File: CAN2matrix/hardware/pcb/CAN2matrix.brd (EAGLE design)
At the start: 41 parts, among them IC1 MEGA8-P, IC2 MCP2515-E/P, IC3 MCP2515-E/P, U1 MCP2551P, U2 MCP2551P, X1 CAN1, X2 CAN2

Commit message: remove erroneous connection between GND and power supply wire at C10
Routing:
- net N$33: track 27.7 -> 28.5 mm
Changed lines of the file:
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@@
 <grid distance="0.05" unitdist="inch" unit="inch" style="lines" multiple="1" display="no" altdistance="0.025" altunitdist="inch" altunit="inch"/>
 <layers>
-<layer number="1" name="Top" color="4" fill="1" visible="yes" active="yes"/>
+<layer number="1" name="Top" color="4" fill="1" visible="no" active="yes"/>
 <layer number="16" name="Bottom" color="1" fill="1" visible="yes" active="yes"/>
 <layer number="17" name="Pads" color="2" fill="1" visible="yes" active="yes"/>
@@
 <wire x1="13.97" y1="72.39" x2="19.05" y2="72.39" width="1.778" layer="16"/>
 <wire x1="19.05" y1="72.39" x2="25.4" y2="72.39" width="1.778" layer="16"/>
-<wire x1="25.4" y1="72.39" x2="26.67" y2="71.12" width="1.778" layer="16"/>
+<wire x1="25.4" y1="72.39" x2="29.21" y2="72.39" width="1.778" layer="16"/>
 <contactref element="SV3" pad="3"/>
-<wire x1="26.67" y1="71.12" x2="26.67" y2="64.77" width="1.778" layer="16"/>
-<wire x1="26.67" y1="64.77" x2="27.94" y2="63.5" width="1.778" layer="16"/>
-<wire x1="27.94" y1="63.5" x2="30.48" y2="63.5" width="1.778" layer="16"/>
+<wire x1="29.21" y1="72.39" x2="29.21" y2="64.77" width="1.778" layer="16"/>
+<wire x1="29.21" y1="64.77" x2="30.48" y2="63.5" width="1.778" layer="16"/>
 </signal>
 </signals>

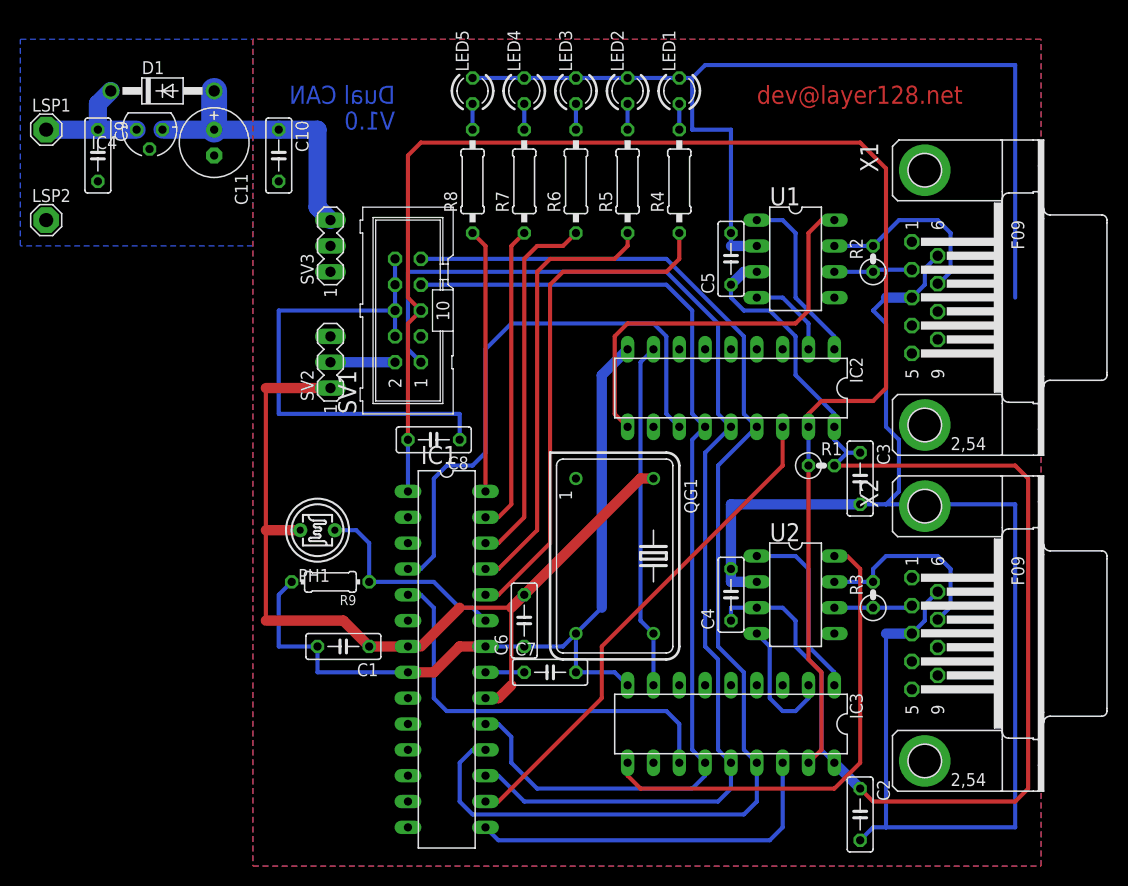
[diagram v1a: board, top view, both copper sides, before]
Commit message: rework top layer to avoid shortcuts with Sub-D connector; solve overlapping error with connector pad
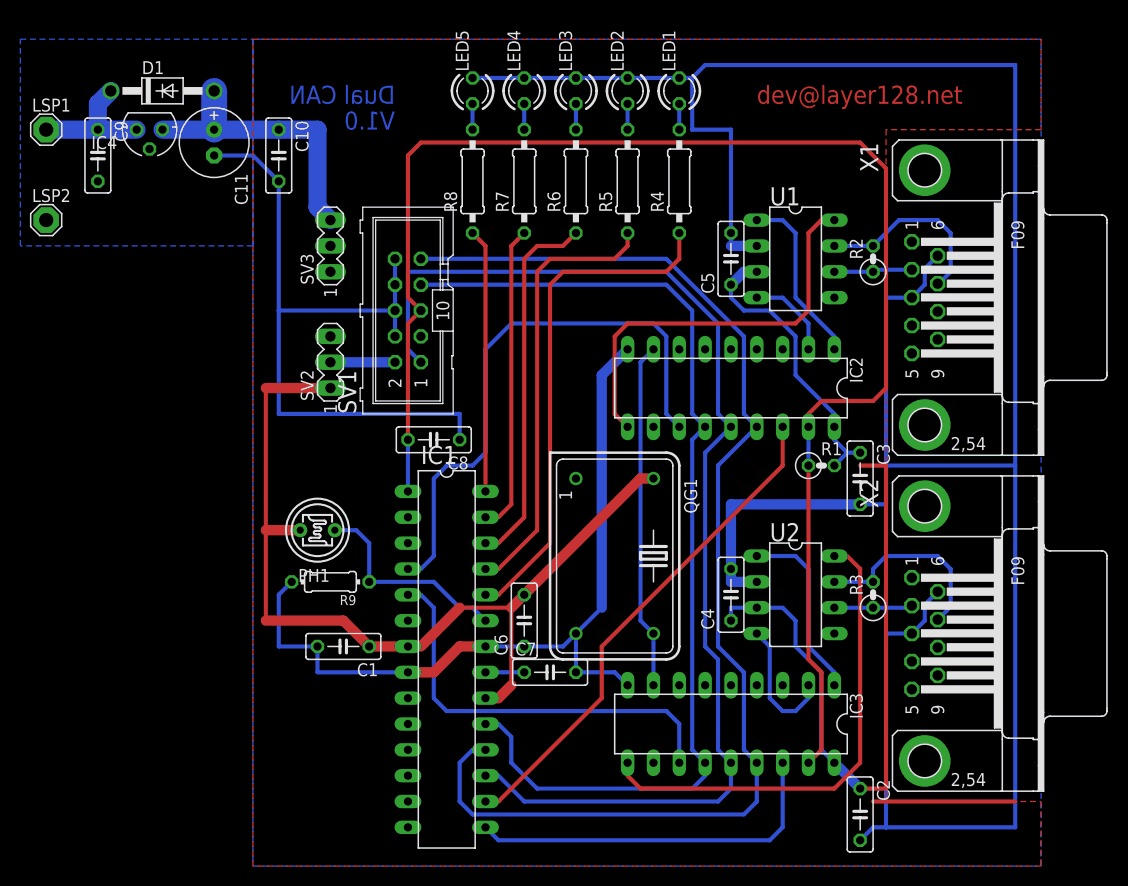
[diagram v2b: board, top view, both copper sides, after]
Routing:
- net GND: track 371.3 -> 409.6 mm
- net +5V: track 213.0 -> 196.2 mm
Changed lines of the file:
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@@
 <grid distance="0.05" unitdist="inch" unit="inch" style="lines" multiple="1" display="no" altdistance="0.025" altunitdist="inch" altunit="inch"/>
 <layers>
-<layer number="1" name="Top" color="4" fill="1" visible="no" active="yes"/>
+<layer number="1" name="Top" color="4" fill="1" visible="yes" active="yes"/>
 <layer number="16" name="Bottom" color="1" fill="1" visible="yes" active="yes"/>
 <layer number="17" name="Pads" color="2" fill="1" visible="yes" active="yes"/>
@@
 <wire x1="49.53" y1="26.67" x2="60.96" y2="38.1" width="1.016" layer="1"/>
 <wire x1="60.96" y1="38.1" x2="62.23" y2="38.1" width="1.016" layer="1"/>
-<wire x1="80.01" y1="39.37" x2="97.79" y2="39.37" width="0.4064" layer="1"/>
-<wire x1="97.79" y1="39.37" x2="99.06" y2="38.1" width="0.4064" layer="1"/>
-<wire x1="99.06" y1="38.1" x2="99.06" y2="7.62" width="0.4064" layer="1"/>
-<wire x1="99.06" y1="7.62" x2="97.79" y2="6.35" width="0.4064" layer="1"/>
 <wire x1="97.79" y1="6.35" x2="83.82" y2="6.35" width="0.4064" layer="1"/>
-<wire x1="83.82" y1="6.35" x2="82.55" y2="7.62" width="0.4064" layer="1"/>
 <wire x1="24.13" y1="33.02" x2="24.13" y2="24.13" width="0.4064" layer="1"/>
 <wire x1="27.51" y1="33.02" x2="24.13" y2="33.02" width="1.016" layer="1"/>
@@
 <wire x1="69.85" y1="57.15" x2="71.12" y2="58.42" width="1.016" layer="16"/>
 <wire x1="71.12" y1="58.42" x2="72.39" y2="58.42" width="1.016" layer="16"/>
+<contactref element="SV3" pad="2"/>
 <polygon width="0.4064" layer="1">
+<vertex x="22.86" y="0"/>
 <vertex x="22.86" y="81.28"/>
-<vertex x="22.86" y="0"/>
+<vertex x="100.33" y="81.28"/>
+<vertex x="100.33" y="72.39"/>
+<vertex x="85.09" y="72.39"/>
+<vertex x="85.09" y="6.35"/>
+<vertex x="100.33" y="6.35"/>
 <vertex x="100.33" y="0"/>
-<vertex x="100.33" y="81.28"/>
 </polygon>
-<contactref element="SV3" pad="2"/>
+<wire x1="82.55" y1="7.62" x2="85.09" y2="7.62" width="0.4064" layer="1"/>
+<wire x1="85.09" y1="7.62" x2="85.09" y2="39.37" width="0.4064" layer="1"/>
+<wire x1="85.09" y1="39.37" x2="82.55" y2="39.37" width="0.4064" layer="1"/>
 </signal>
 <signal name="GND">
@@
 <wire x1="83.82" y1="3.81" x2="85.09" y2="3.81" width="0.4064" layer="16"/>
 <wire x1="85.09" y1="3.81" x2="97.79" y2="3.81" width="0.4064" layer="16"/>
-<wire x1="97.79" y1="3.81" x2="97.79" y2="35.56" width="0.4064" layer="16"/>
-<wire x1="82.55" y1="35.56" x2="85.09" y2="35.56" width="0.4064" layer="16"/>
-<wire x1="85.09" y1="35.56" x2="97.79" y2="35.56" width="0.4064" layer="16"/>
 <wire x1="64.77" y1="77.47" x2="59.69" y2="77.47" width="0.4064" layer="16"/>
 <wire x1="59.69" y1="77.47" x2="54.61" y2="77.47" width="0.4064" layer="16"/>
@@
 <wire x1="66.04" y1="77.47" x2="67.31" y2="78.74" width="0.4064" layer="16"/>
 <wire x1="67.31" y1="78.74" x2="97.79" y2="78.74" width="0.4064" layer="16"/>
-<wire x1="97.79" y1="78.74" x2="97.79" y2="55.88" width="0.4064" layer="16"/>
 <wire x1="38.1" y1="19.05" x2="40.64" y2="19.05" width="1.016" layer="1"/>
 <wire x1="40.64" y1="19.05" x2="43.18" y2="21.59" width="1.016" layer="1"/>
@@
 <wire x1="57.15" y1="48.26" x2="57.15" y2="25.4" width="1.016" layer="16"/>
 <wire x1="57.15" y1="25.4" x2="54.61" y2="22.86" width="0.4064" layer="16"/>
-<wire x1="85.09" y1="55.88" x2="87.63" y2="55.88" width="1.016" layer="16"/>
-<wire x1="87.63" y1="22.86" x2="85.09" y2="22.86" width="1.016" layer="16"/>
+<wire x1="87.63" y1="22.86" x2="85.09" y2="22.86" width="0.4064" layer="16"/>
 <wire x1="85.09" y1="22.86" x2="85.09" y2="3.81" width="0.4064" layer="16"/>
-<wire x1="85.09" y1="55.88" x2="83.82" y2="54.61" width="0.4064" layer="16"/>
-<wire x1="83.82" y1="54.61" x2="85.09" y2="53.34" width="0.4064" layer="16"/>
-<wire x1="85.09" y1="53.34" x2="85.09" y2="43.18" width="0.4064" layer="16"/>
-<wire x1="85.09" y1="43.18" x2="86.36" y2="41.91" width="0.4064" layer="16"/>
-<wire x1="86.36" y1="41.91" x2="86.36" y2="36.83" width="0.4064" layer="16"/>
-<wire x1="86.36" y1="36.83" x2="85.09" y2="35.56" width="0.4064" layer="16"/>
 <wire x1="43.18" y1="41.91" x2="43.18" y2="44.45" width="0.4064" layer="16"/>
 <wire x1="43.18" y1="44.45" x2="25.4" y2="44.45" width="0.4064" layer="16"/>
@@
 <vertex x="22.86" y="60.96"/>
 </polygon>
+<wire x1="97.79" y1="78.74" x2="97.79" y2="39.37" width="0.4064" layer="16"/>
+<wire x1="97.79" y1="39.37" x2="97.79" y2="3.81" width="0.4064" layer="16"/>
+<wire x1="87.63" y1="55.88" x2="85.09" y2="55.88" width="0.4064" layer="16"/>
+<wire x1="25.4" y1="54.61" x2="25.4" y2="67.31" width="0.4064" layer="16"/>
+<wire x1="25.4" y1="67.31" x2="22.86" y2="69.85" width="0.4064" layer="16"/>
+<wire x1="22.86" y1="69.85" x2="19.05" y2="69.85" width="0.4064" layer="16"/>
+<wire x1="85.09" y1="39.37" x2="97.79" y2="39.37" width="0.4064" layer="16"/>
+<wire x1="82.55" y1="35.56" x2="85.09" y2="35.56" width="0.4064" layer="16"/>
+<wire x1="85.09" y1="35.56" x2="85.09" y2="39.37" width="0.4064" layer="16"/>
+<wire x1="85.09" y1="39.37" x2="85.09" y2="55.88" width="0.4064" layer="16"/>
 </signal>
 <signal name="N$4">
